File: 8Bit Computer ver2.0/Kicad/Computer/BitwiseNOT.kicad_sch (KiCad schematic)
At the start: 5 parts, among them IC10 SN74AHC74DR, IC13 SN74ABT574ADWR, IC41 SN74LVC1G14DBVR, IC60 SN74AHC14DR, IC61 SN74AHC14DR

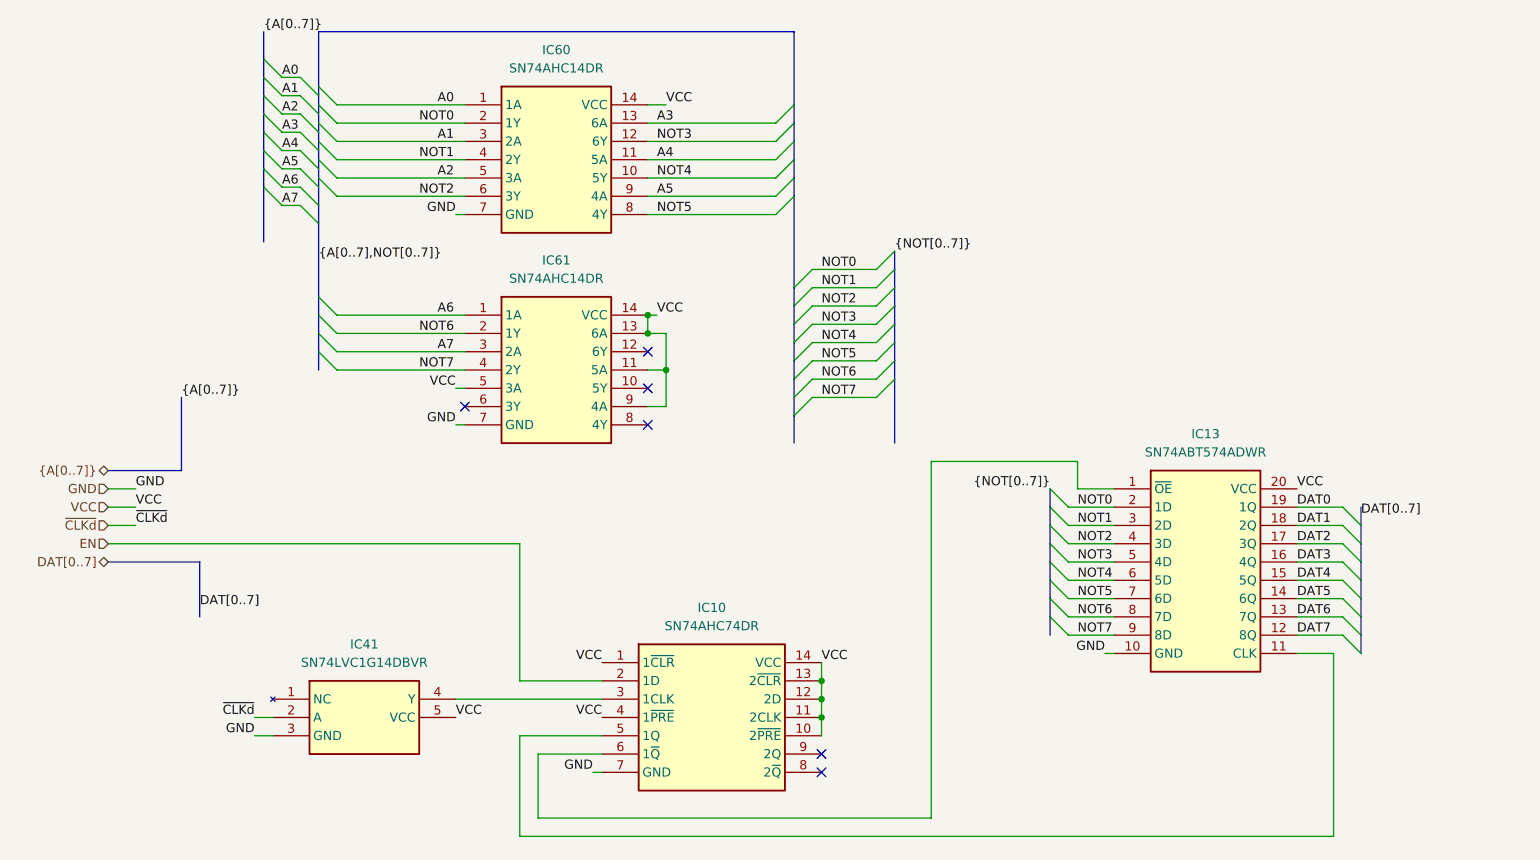
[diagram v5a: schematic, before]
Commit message: Kicad SCH/PCB
Kicad SCH/PCB:
changed the References in SCH
began with INOUTPUT module nearly done
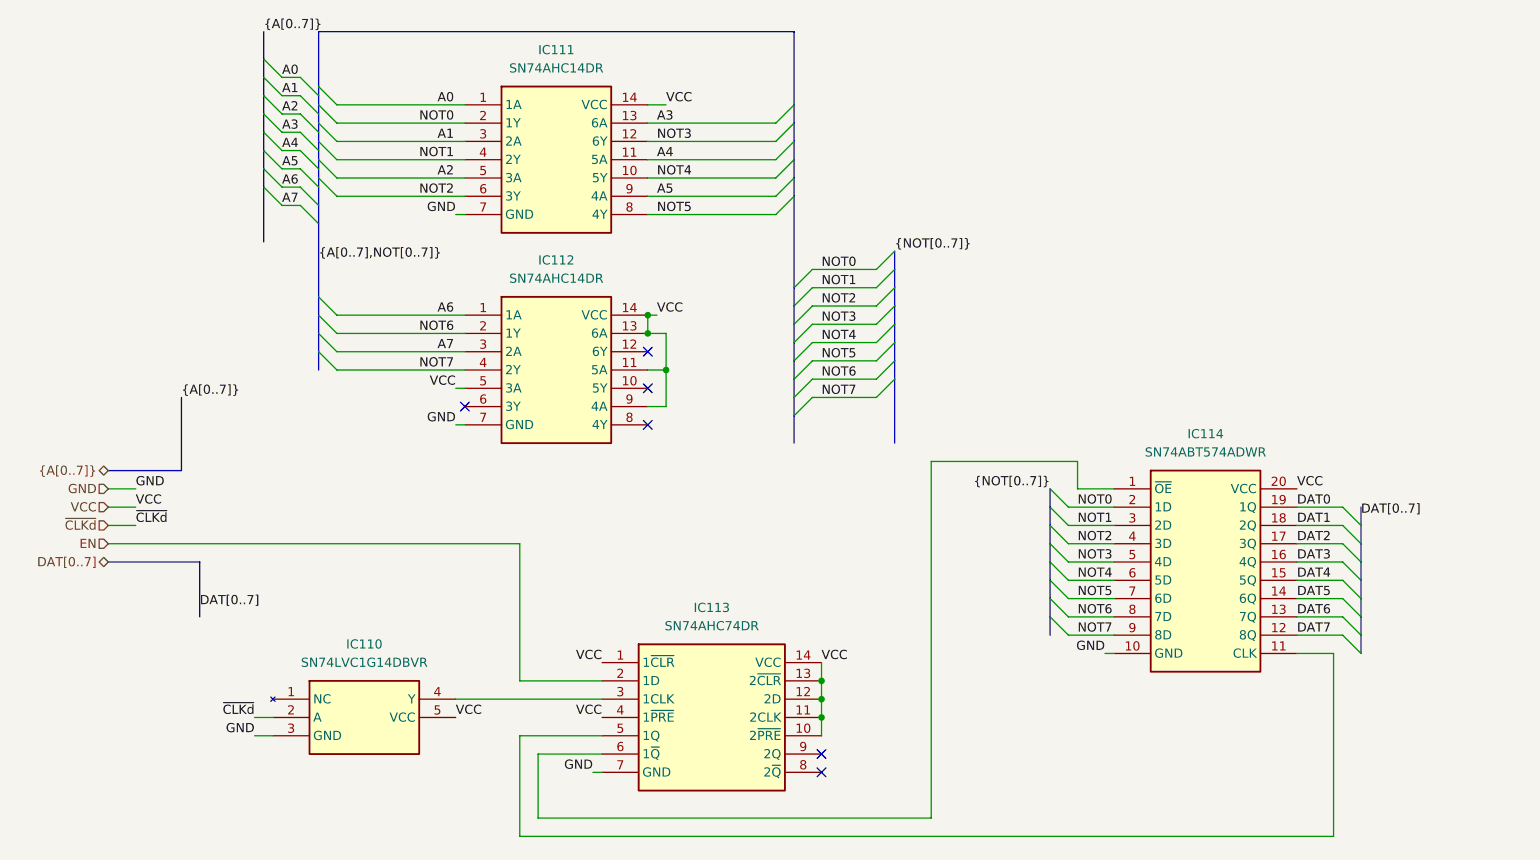
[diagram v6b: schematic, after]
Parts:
- renumbered IC41 to IC110, IC60 to IC111, IC61 to IC112, IC10 to IC113, IC13 to IC114
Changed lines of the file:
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@@
 		(dnp no)
 		(fields_autoplaced yes)
-		(property "Reference" "IC10"
+		(property "Reference" "IC113"
 			(at 128.27 119.38 0)
 			(effects
@@
 			(project "Computer"
 				(path "/1196a00e-6878-4d6d-82b7-9e052dfe7c14/c4d8b530-1c6d-45af-88d2-7dc1d4321a34/ea379de7-167f-4681-88e3-fa025ade4a21"
-					(reference "IC10")
+					(reference "IC113")
 					(unit 1)
 				)
@@
 		(dnp no)
 		(fields_autoplaced yes)
-		(property "Reference" "IC61"
+		(property "Reference" "IC112"
 			(at 106.68 71.12 0)
 			(effects
@@
 			(project "Computer"
 				(path "/1196a00e-6878-4d6d-82b7-9e052dfe7c14/c4d8b530-1c6d-45af-88d2-7dc1d4321a34/ea379de7-167f-4681-88e3-fa025ade4a21"
-					(reference "IC61")
+					(reference "IC112")
 					(unit 1)
 				)
@@
 		(dnp no)
 		(fields_autoplaced yes)
-		(property "Reference" "IC60"
+		(property "Reference" "IC111"
 			(at 106.68 41.91 0)
 			(effects
@@
 			(project "Computer"
 				(path "/1196a00e-6878-4d6d-82b7-9e052dfe7c14/c4d8b530-1c6d-45af-88d2-7dc1d4321a34/ea379de7-167f-4681-88e3-fa025ade4a21"
-					(reference "IC60")
+					(reference "IC111")
 					(unit 1)
 				)
@@
 		(dnp no)
 		(fields_autoplaced yes)
-		(property "Reference" "IC41"
+		(property "Reference" "IC110"
 			(at 80.01 124.46 0)
 			(effects
@@
 			(project "Computer"
 				(path "/1196a00e-6878-4d6d-82b7-9e052dfe7c14/c4d8b530-1c6d-45af-88d2-7dc1d4321a34/ea379de7-167f-4681-88e3-fa025ade4a21"
-					(reference "IC41")
+					(reference "IC110")
 					(unit 1)
 				)
@@
 		(dnp no)
 		(fields_autoplaced yes)
-		(property "Reference" "IC13"
+		(property "Reference" "IC114"
 			(at 196.85 95.25 0)
 			(effects
@@
 			(project "Computer"
 				(path "/1196a00e-6878-4d6d-82b7-9e052dfe7c14/c4d8b530-1c6d-45af-88d2-7dc1d4321a34/ea379de7-167f-4681-88e3-fa025ade4a21"
-					(reference "IC13")
+					(reference "IC114")
 					(unit 1)
 				)

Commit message: changed page numbers, compressed ROOT file from A1 to A4
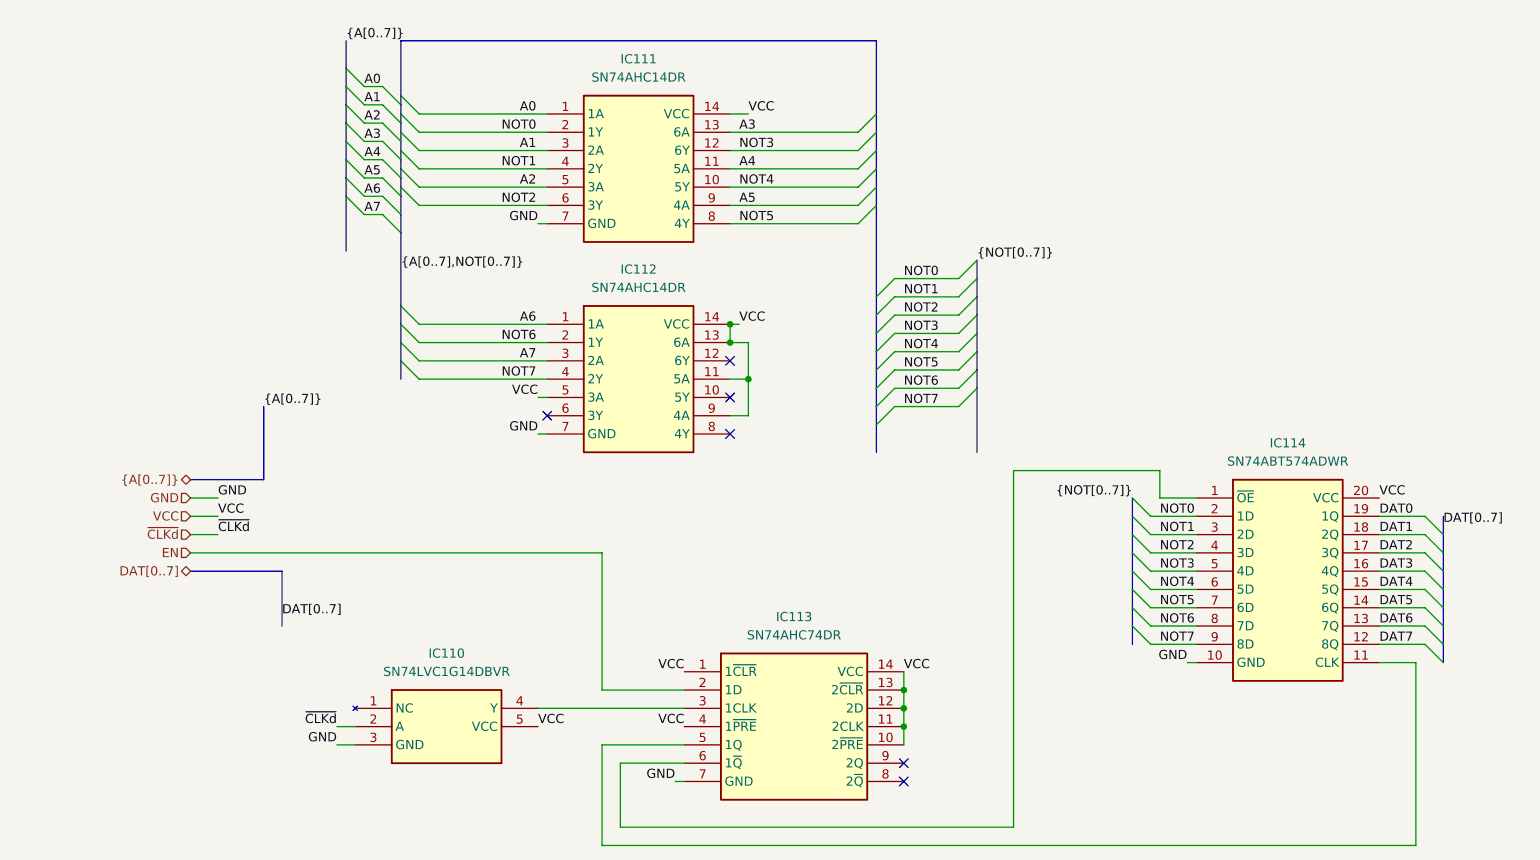
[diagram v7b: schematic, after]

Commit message: changed page numbers, every schematic is now A4
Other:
- title: (none) -> ${SHEETNAME}
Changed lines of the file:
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@@
 	(generator_version "9.0")
 	(paper "A4")
+	(title_block
+		(title "${SHEETNAME}")
+		(date "2026-03-21")
+		(rev "2.7")
+	)
 	(junction
 		(at 130.81 80.01)
